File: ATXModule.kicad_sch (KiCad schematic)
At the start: 14 parts, among them J1 Screw_Terminal_01x02, J2 Screw_Terminal_01x02, J3 Screw_Terminal_01x02, J4 Conn_01x02_Pin, Q1 2N2222A, Q2 2N2222A

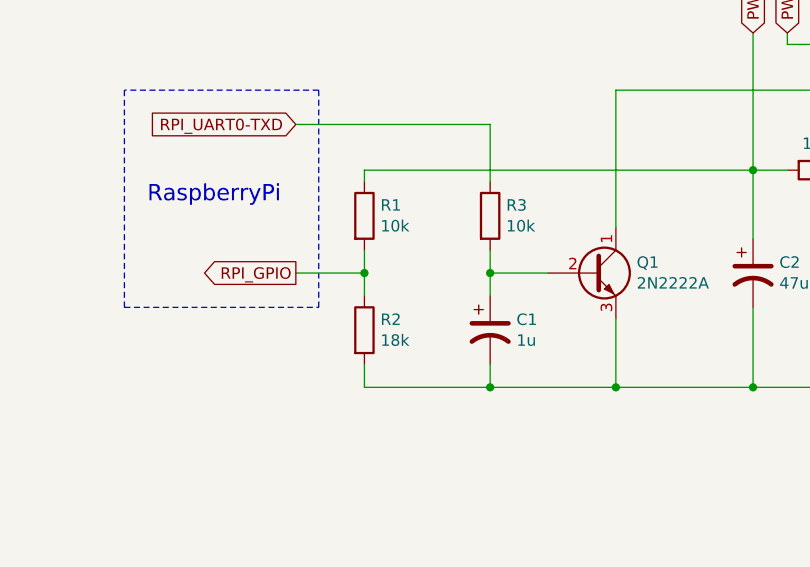
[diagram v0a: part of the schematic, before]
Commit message: Fix to support RaspberryPi 4
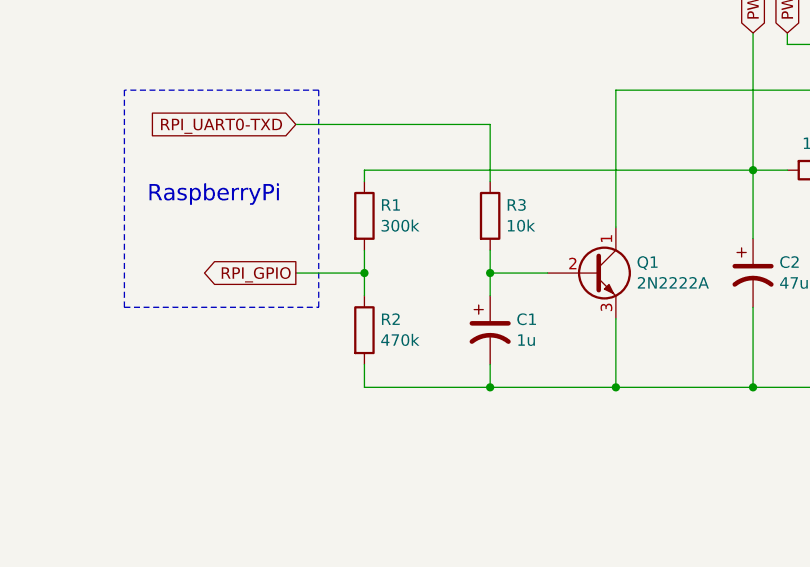
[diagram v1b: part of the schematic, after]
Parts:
- R1: value 10k -> 300k
- R2: value 18k -> 470k
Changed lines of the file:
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@@
 			)
 		)
-		(property "Value" "10k"
+		(property "Value" "300k"
 			(at 113.538 62.103 0)
 			(effects
@@
 			)
 		)
-		(property "Value" "18k"
+		(property "Value" "470k"
 			(at 113.538 74.803 0)
 			(effects

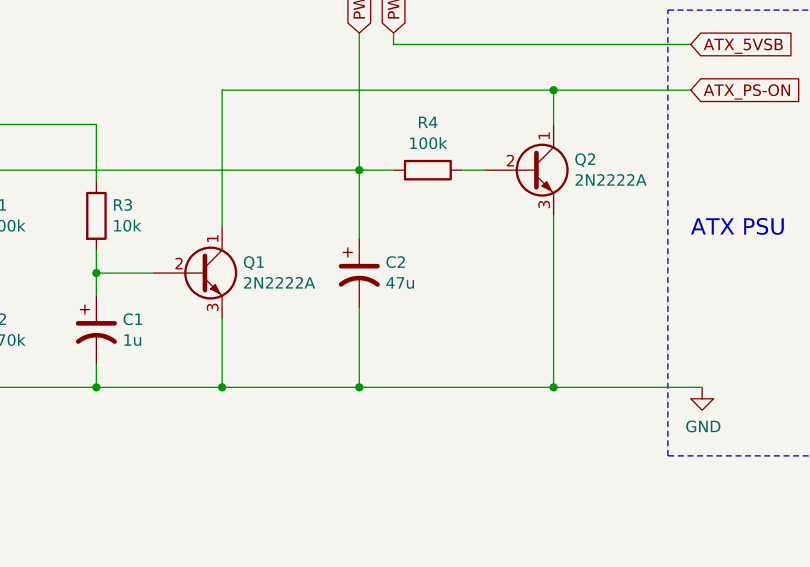
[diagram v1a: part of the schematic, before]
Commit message: 33u capacitor is enough
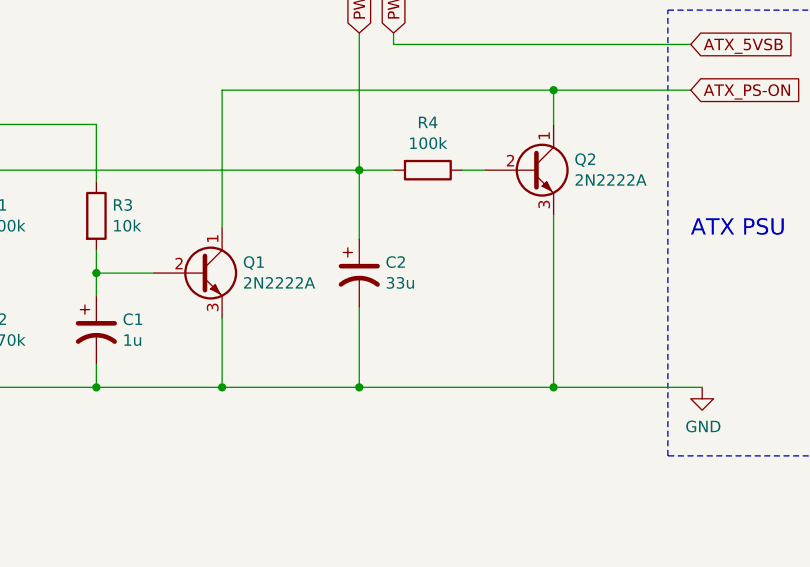
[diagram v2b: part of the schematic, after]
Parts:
- C2: value 47u -> 33u
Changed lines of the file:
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@@
 			)
 		)
-		(property "Value" "47u"
+		(property "Value" "33u"
 			(at 157.861 68.453 0)
 			(effects

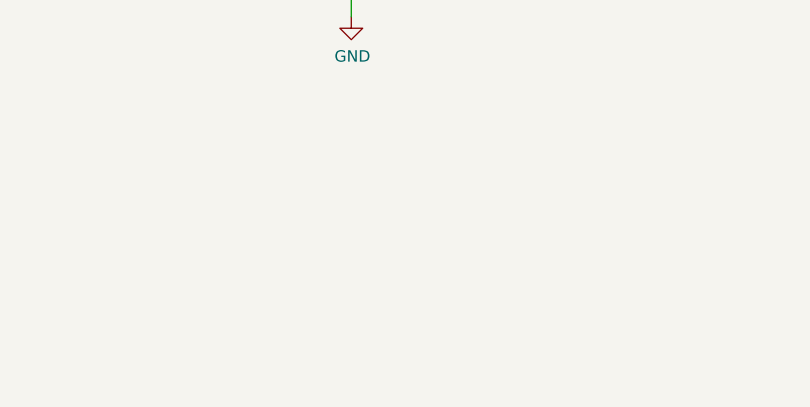
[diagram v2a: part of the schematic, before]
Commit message: Add fan footprint, screw holes and connectors
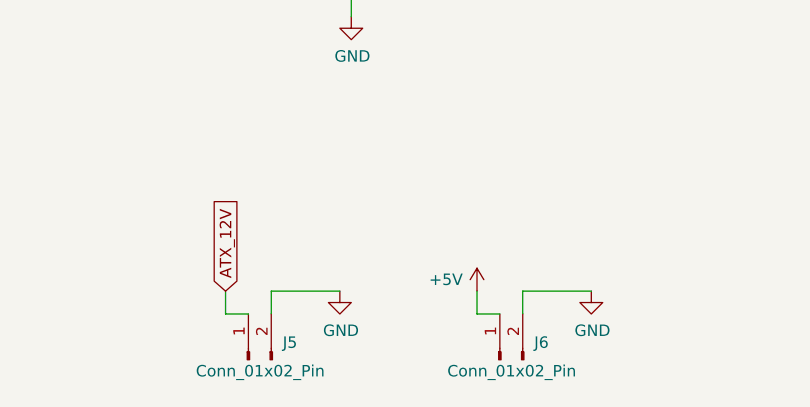
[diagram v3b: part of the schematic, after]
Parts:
- added J5, J6: Conn_01x02_Pin, Connector_PinSocket_2.54mm:PinSocket_2x01_P2.54mm_Vertical_SMD, symbol Connector:Conn_01x02_Pin
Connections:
- net +5V: now also J6.1 (Pin_1)
- net ATX_12V: now also J5.1 (Pin_1)
- net GND: now also J5.2 (Pin_2), J6.2 (Pin_2)
